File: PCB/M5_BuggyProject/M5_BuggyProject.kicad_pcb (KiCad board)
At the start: 2 copper layers, 50.8 x 99.1 mm, 28 parts, among them J1 XT60, J2 VCC, J3 10V, J4 Receiver

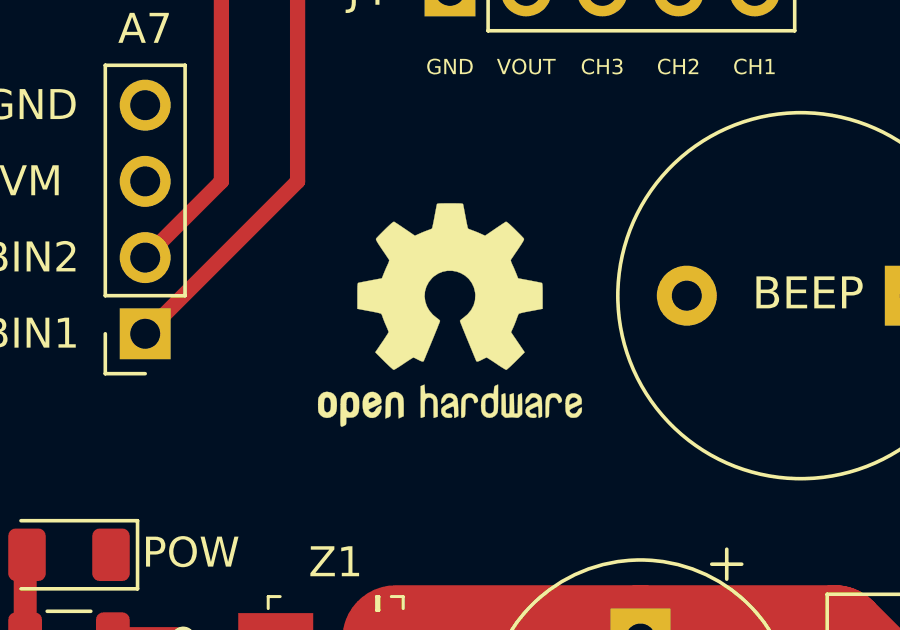
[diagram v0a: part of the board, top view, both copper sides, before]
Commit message: Updated PCB, removed gerbers
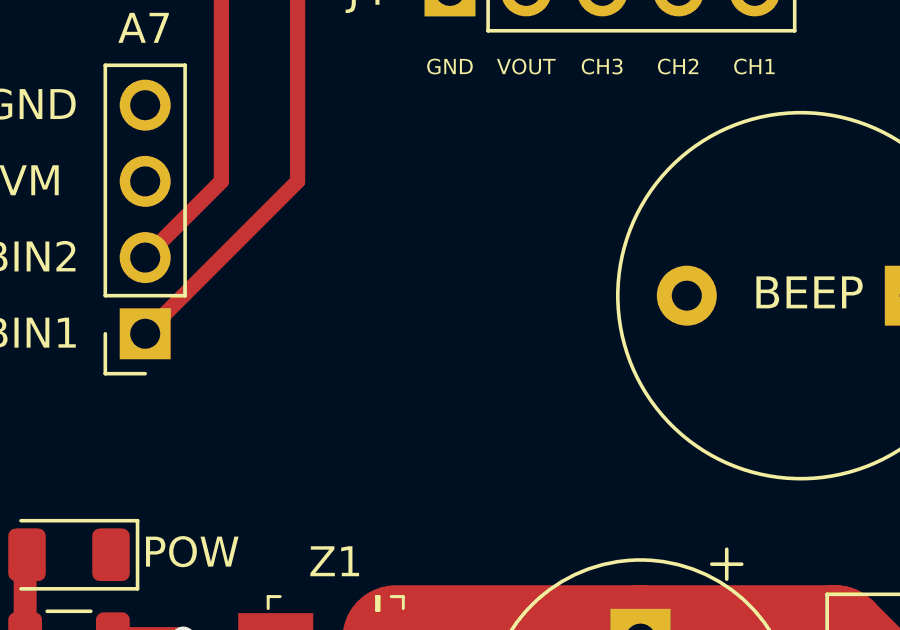
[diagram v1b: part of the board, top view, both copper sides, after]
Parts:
- removed REF**: OSHW-Logo2_9.8x8mm_SilkScreen, Symbol:OSHW-Logo2_9.8x8mm_SilkScreen

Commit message: Started PCB v2
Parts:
- removed D2, D4: ORANGE, LED_SMD:LED_1206_3216Metric
- removed the G*** at (73.9, 111.1)
- removed R2, R3: 100, Resistor_SMD:R_1206_3216Metric
- added J5: GND, TestPoint:TestPoint_Plated_Hole_D5.0mm, F.Cu at (130.0, 136.9)
- added J6: AIN1, Connector_PinSocket_2.54mm:PinSocket_1x02_P2.54mm_Vertical, F.Cu at (183.4, 81.0)
- added J7: AIN2, Connector_PinSocket_2.54mm:PinSocket_1x02_P2.54mm_Vertical, F.Cu at (183.4, 111.5)
- added J8: BIN1, Connector_PinSocket_2.54mm:PinSocket_1x02_P2.54mm_Vertical, F.Cu at (122.4, 78.5)
- added J9: BIN2, Connector_PinSocket_2.54mm:PinSocket_1x02_P2.54mm_Vertical, F.Cu at (122.4, 109.0)
- H1, H2, H3, H4: footprint MountingHole:MountingHole_3.2mm_M3_Pad_Via -> MountingHole:MountingHole_4.3mm_M4_Pad_Via
- J2, J3: footprint TestPoint:TestPoint_Loop_D1.80mm_Drill1.0mm_Beaded -> TestPoint:TestPoint_Plated_Hole_D5.0mm
- Z1: value Diode -> Zener
- moved H4 116.4 mm to (188.5, 149.6)
- moved Z1 85.2 mm to (168.9, 124.2), turned to 0 degrees
- moved D3 83.8 mm to (158.0, 124.0)
- moved R1 83.8 mm to (158.0, 126.7)
- moved J4 80.3 mm to (140.2, 147.1), turned to 270 degrees
- moved A4 76.1 mm to (183.4, 121.7)
- moved D1 74.0 mm to (173.2, 131.8)
- moved A3 72.3 mm to (183.4, 91.2)
- moved C1 71.9 mm to (163.1, 131.8)
- moved H2 70.3 mm to (188.5, 37.8)
- moved A2 69.7 mm to (183.3, 60.7)
- moved G*** 67.0 mm to (152.9, 111.5)
- moved J1 66.2 mm to (166.0, 147.1), turned to 0 degrees
- moved J3 57.8 mm to (152.9, 136.9)
- moved J2 57.5 mm to (152.9, 147.1)
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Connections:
- A1 pad 10: CONFIG_L -> Net-(A1-Pad10)
- A1 pad 9: CONFIG_R -> Net-(A1-Pad9)
- H1 pad 1: GND -> Net-(H1-Pad1)
- H2 pad 1: GND -> Net-(H2-Pad1)
- H3 pad 1: GND -> Net-(H3-Pad1)
- H4 pad 1: GND -> Net-(H4-Pad1)
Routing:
- net AIN2: track 54.3 -> 126.0 mm
- net AIN1: track 50.3 -> 114.2 mm, vias 1 -> 0
- net BIN1: track 77.0 -> 135.3 mm
- net BIN2: track 77.4 -> 128.6 mm, vias 0 -> 1
- net CHANNEL_2: track 36.0 -> 86.2 mm
- net CHANNEL_3: track 32.6 -> 82.6 mm
- net CHANNEL_1: track 39.6 -> 89.1 mm
- net +3V3: track 51.2 -> 98.2 mm, vias 1 -> 0
- net CONFIG_L: track 27.4 -> 0.00 mm, vias 1 -> 0
- net CONFIG_R: track 22.6 -> 0.00 mm, vias 1 -> 0
- net VCC: track 16.8 -> 37.2 mm
- net +10V: track 18.6 -> 38.2 mm, vias 1 -> 0
- net Net-(D3-Pad2): track 2.82 -> 0.09 mm
- net Net-(D2-Pad1): track 2.65 -> 0.00 mm
- net Net-(D4-Pad1): track 2.57 -> 0.00 mm
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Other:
- board size 50.8 x 99.1 mm -> 81.3 x 121.9 mm
- board text added: "#UMassAmherstM5 @UMassAmherstM5"
- board text added: "All-Terrain Buggy"
- board text added: "DRV8871"
- board text added: "Feather Breakout"
- board text added: "Power Electronics"
- board text added: "Radio Receiver"
- board text added: "VIN"
- board text added: "v2.0"
- board text removed: "#UMassAmherstM5"
- board text removed: "-"
- board text removed: "@UMassAmherstM5"
- board text removed: "All-Terrain Buggy v1.0"
- board text removed: "CON_L"
- board text removed: "CON_R"
- board text removed: "VOUT"

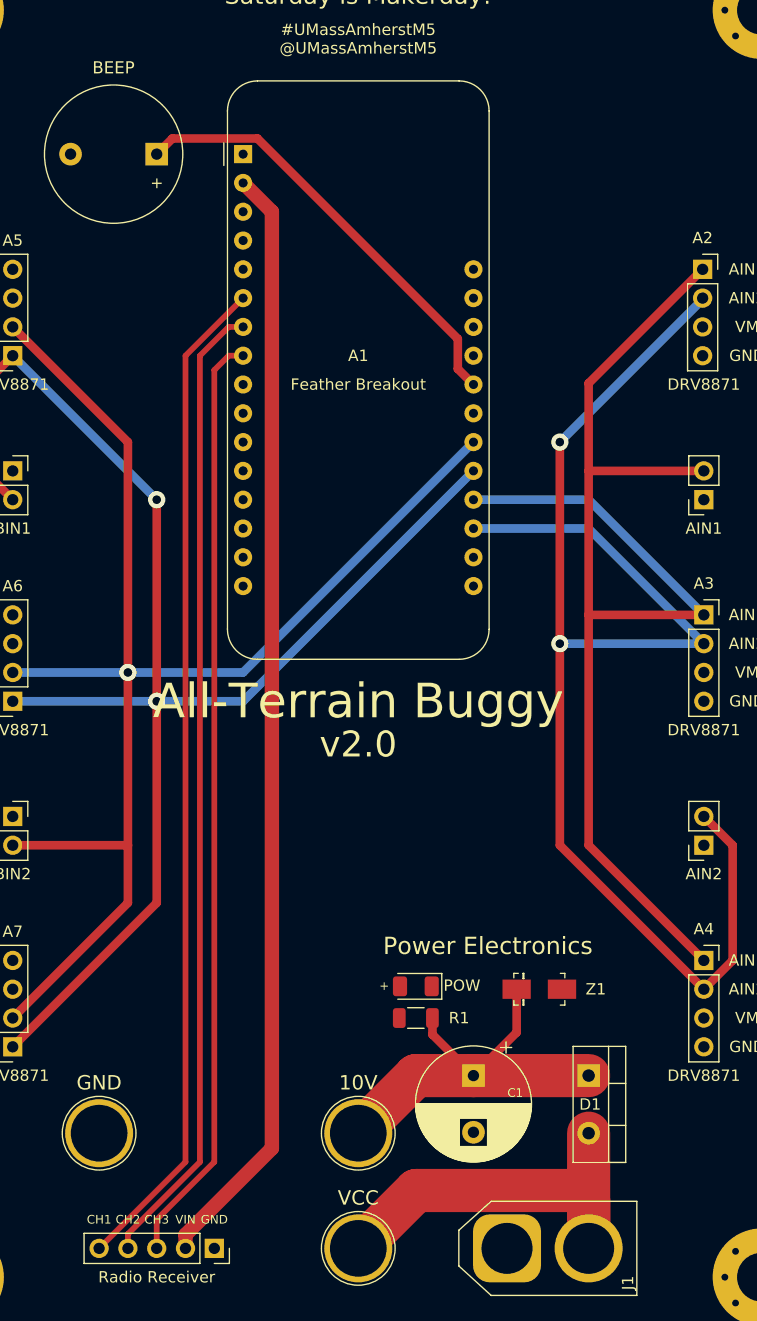
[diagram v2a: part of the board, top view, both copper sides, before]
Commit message: Added UMass logo, moved things around
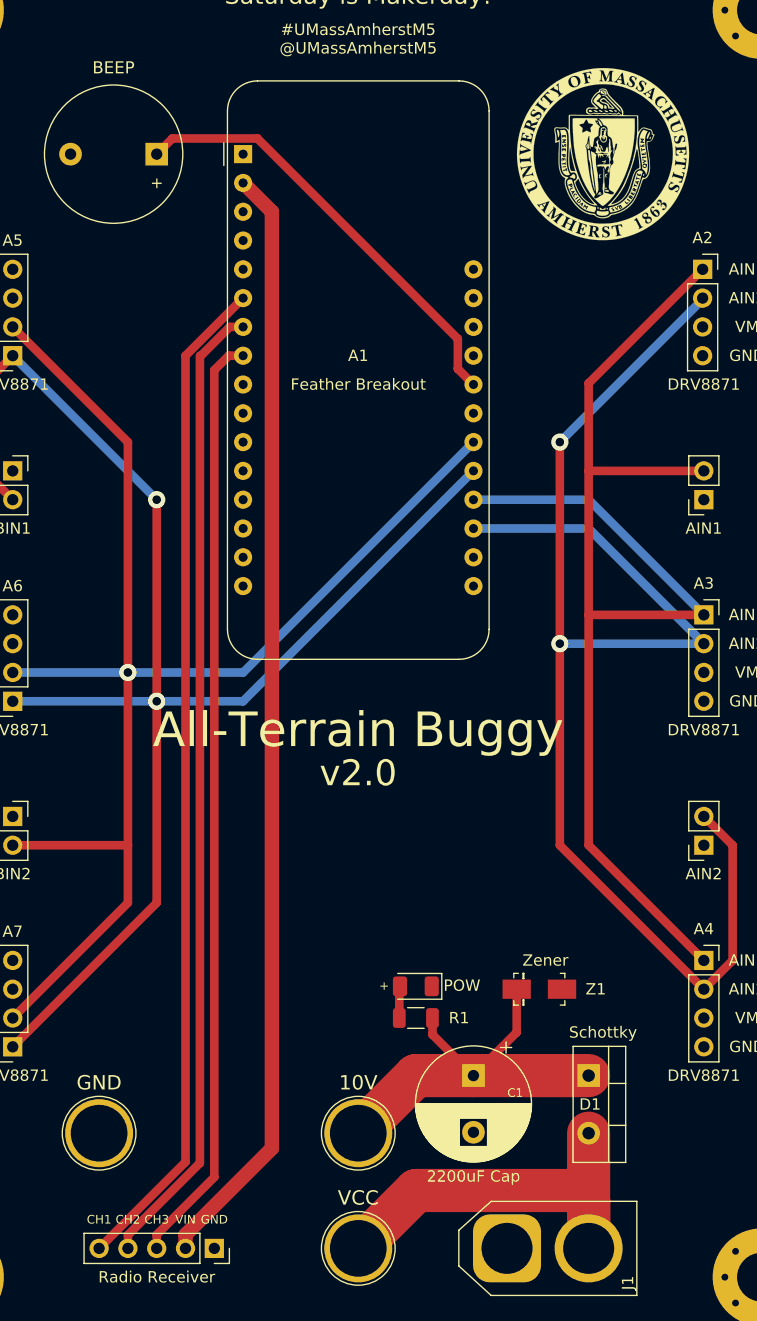
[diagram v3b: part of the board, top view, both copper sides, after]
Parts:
- added G***: LOGO, Figures:UMass_logo, F.Cu at (174.5, 50.5)
- moved G*** 2.54 mm to (152.9, 114.0)
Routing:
- net Net-(D3-Pad2): track 0.09 -> 2.82 mm
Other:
- board text added: "2200uF Cap"
- board text added: "Schottky"
- board text added: "Zener"
- board text removed: "Power Electronics"

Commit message: Updated PCB
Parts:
- removed the G*** at (174.5, 50.5)
- removed J2: VCC, TestPoint:TestPoint_Plated_Hole_D5.0mm
- added SW1: SW_SPDT, Buggy_Footprints:1101M2S3CQE2, F.Cu at (173.2, 138.2)
- moved J5 25.0 mm to (152.9, 147.1)
- moved Z1 8.29 mm to (165.6, 116.6)
- moved D3 7.69 mm to (150.4, 122.9)
- moved R1 7.62 mm to (150.4, 126.7)
- moved C1 7.62 mm to (163.1, 124.2)
- moved D1 7.62 mm to (173.2, 124.2)
- moved G*** 1.91 mm to (152.9, 112.1)
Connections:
- D1 pad 2: VCC -> Net-(D1-Pad2)
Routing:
- net +10V: track 38.2 -> 394.9 mm, vias 0 -> 2
- net VCC: track 37.2 -> 8.89 mm
- net BIN1: track 135.3 -> 149.5 mm
- net Net-(D1-Pad2): track 0.00 -> 10.8 mm
- net AIN1: track 114.2 -> 107.0 mm
- net BIN2: track 128.6 -> 131.6 mm, vias 1 -> 0
- net BEEP: track 39.1 -> 36.4 mm
- net AIN2: track 126.0 -> 127.5 mm
- net Net-(D3-Pad2): track 2.82 -> 3.84 mm
- net CHANNEL_3: track 82.6 -> 81.9 mm
- net CHANNEL_2: track 86.2 -> 85.5 mm
- net GND: vias 0 -> 2
- added copper zone on B.Cu, net GND
- removed copper zone on B.Cu, net +10V
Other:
- board text added: "2200uF"
- board text added: "JST Power"
- board text added: "OFF"
- board text added: "ON"
- board text added: "Power Switch"
- board text added: "XT60"
- board text removed: "+"
- board text removed: "2200uF Cap"
- board text removed: "VCC"

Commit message: Updated document dates
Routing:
- net +10V: track 394.9 -> 390.7 mm

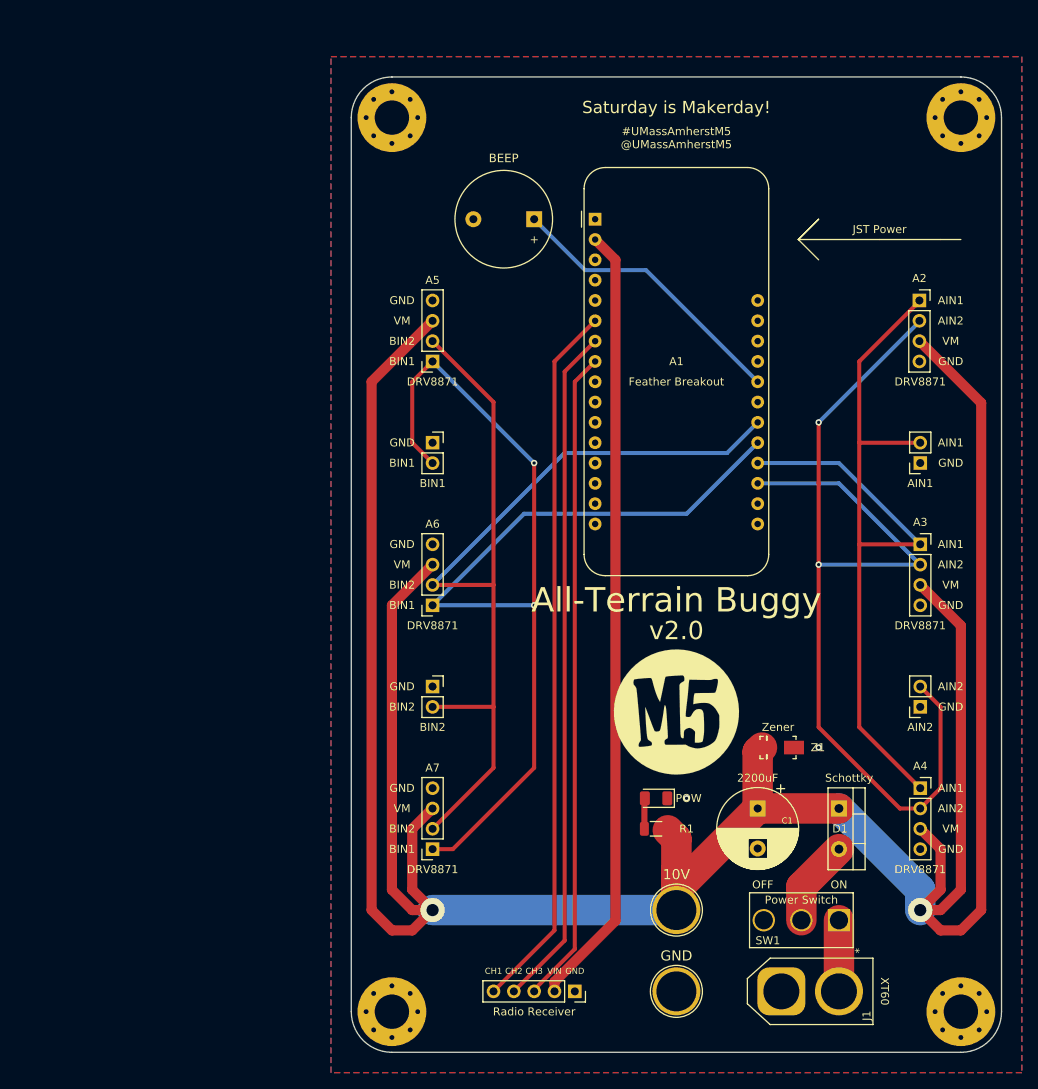
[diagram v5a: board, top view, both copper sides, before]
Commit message: Imported to KiCad 6
We're now in KiCad 6 land.
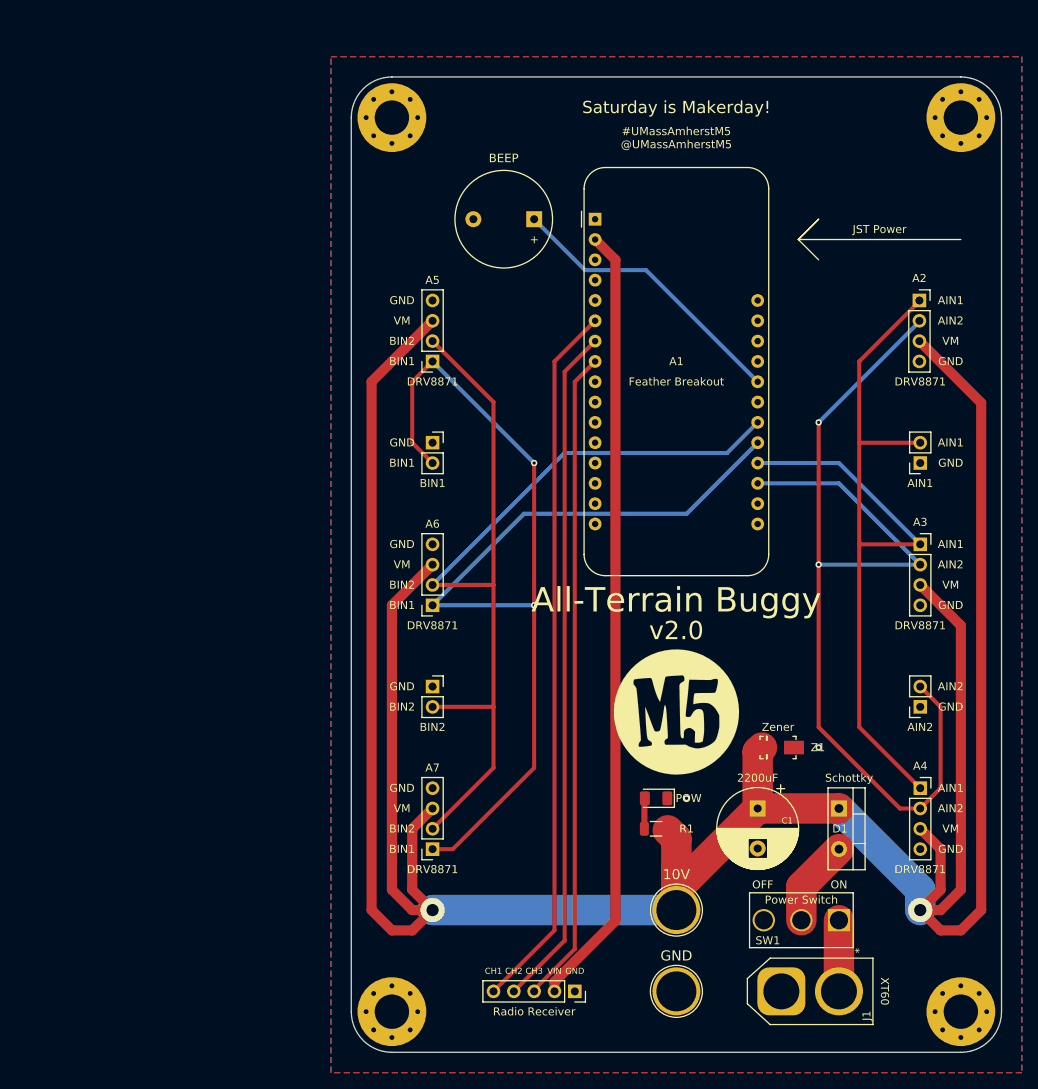
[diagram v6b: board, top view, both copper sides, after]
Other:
- net class Default removed
